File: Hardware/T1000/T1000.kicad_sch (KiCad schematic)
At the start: 8 parts, among them J7 Micro_SD_Card_Det1, U1 SAM-M8Q, U6 MS5607-02BA

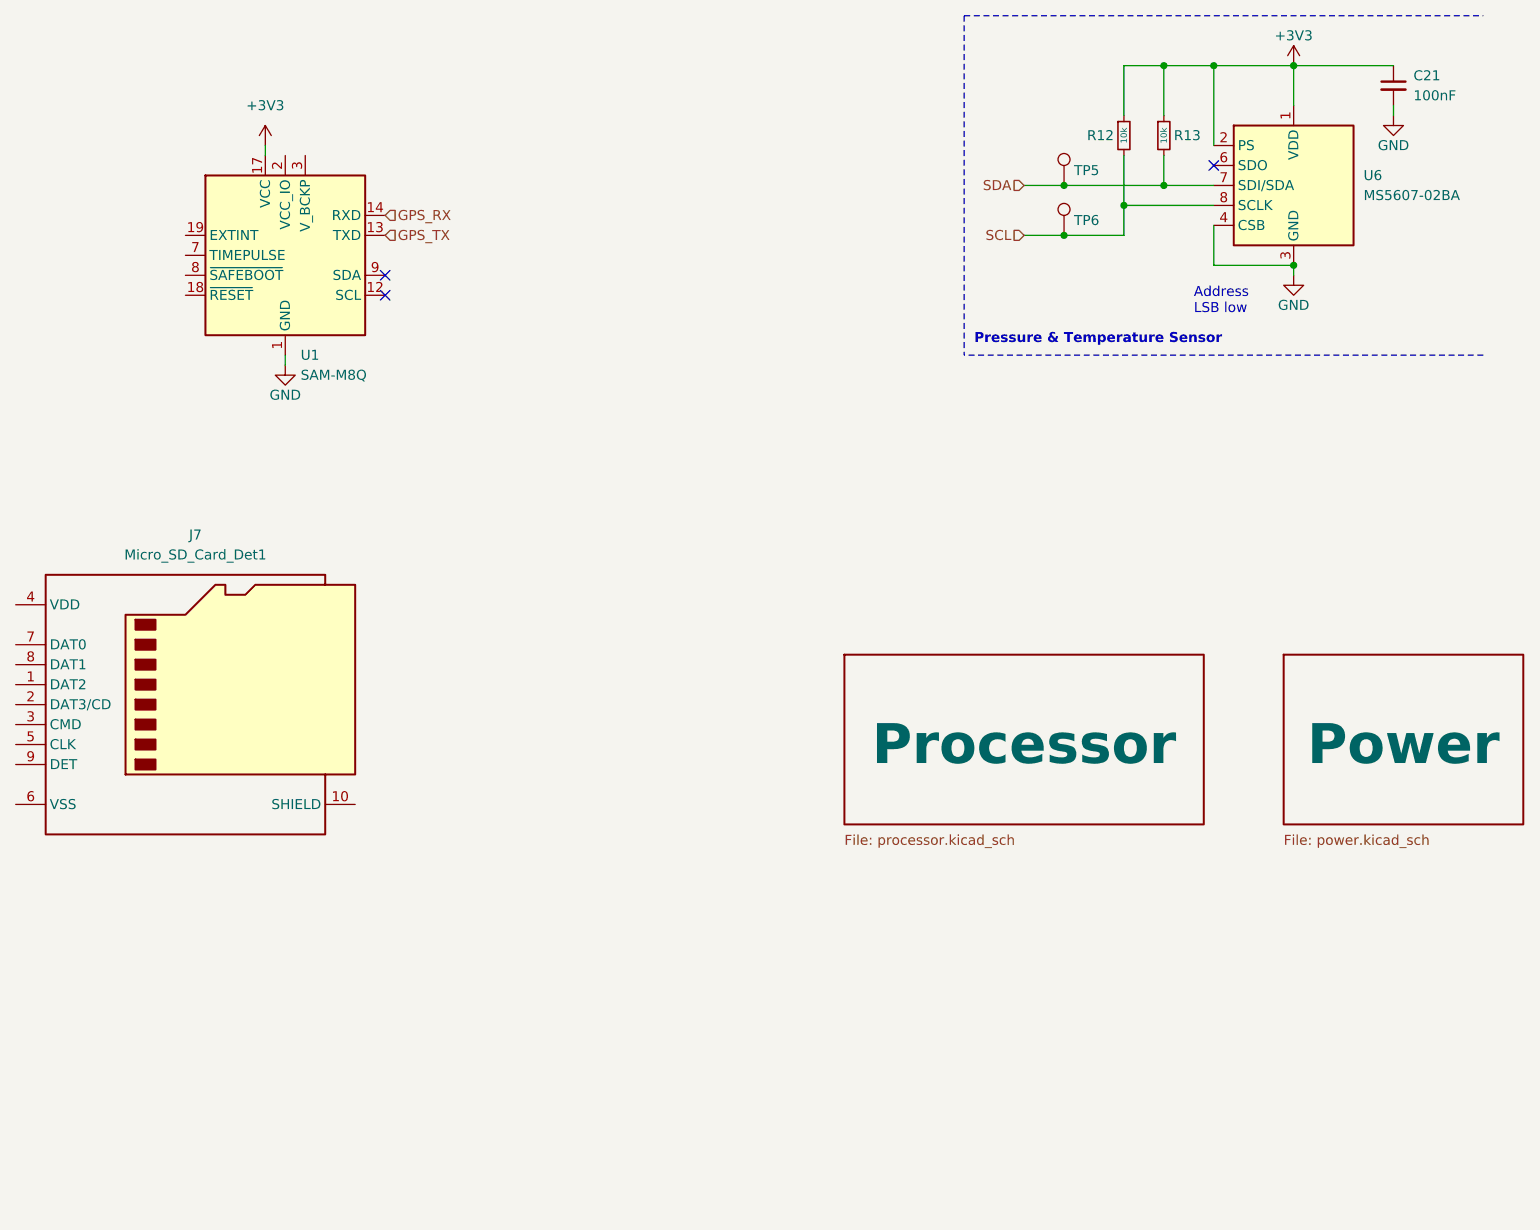
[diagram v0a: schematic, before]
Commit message: added SD card
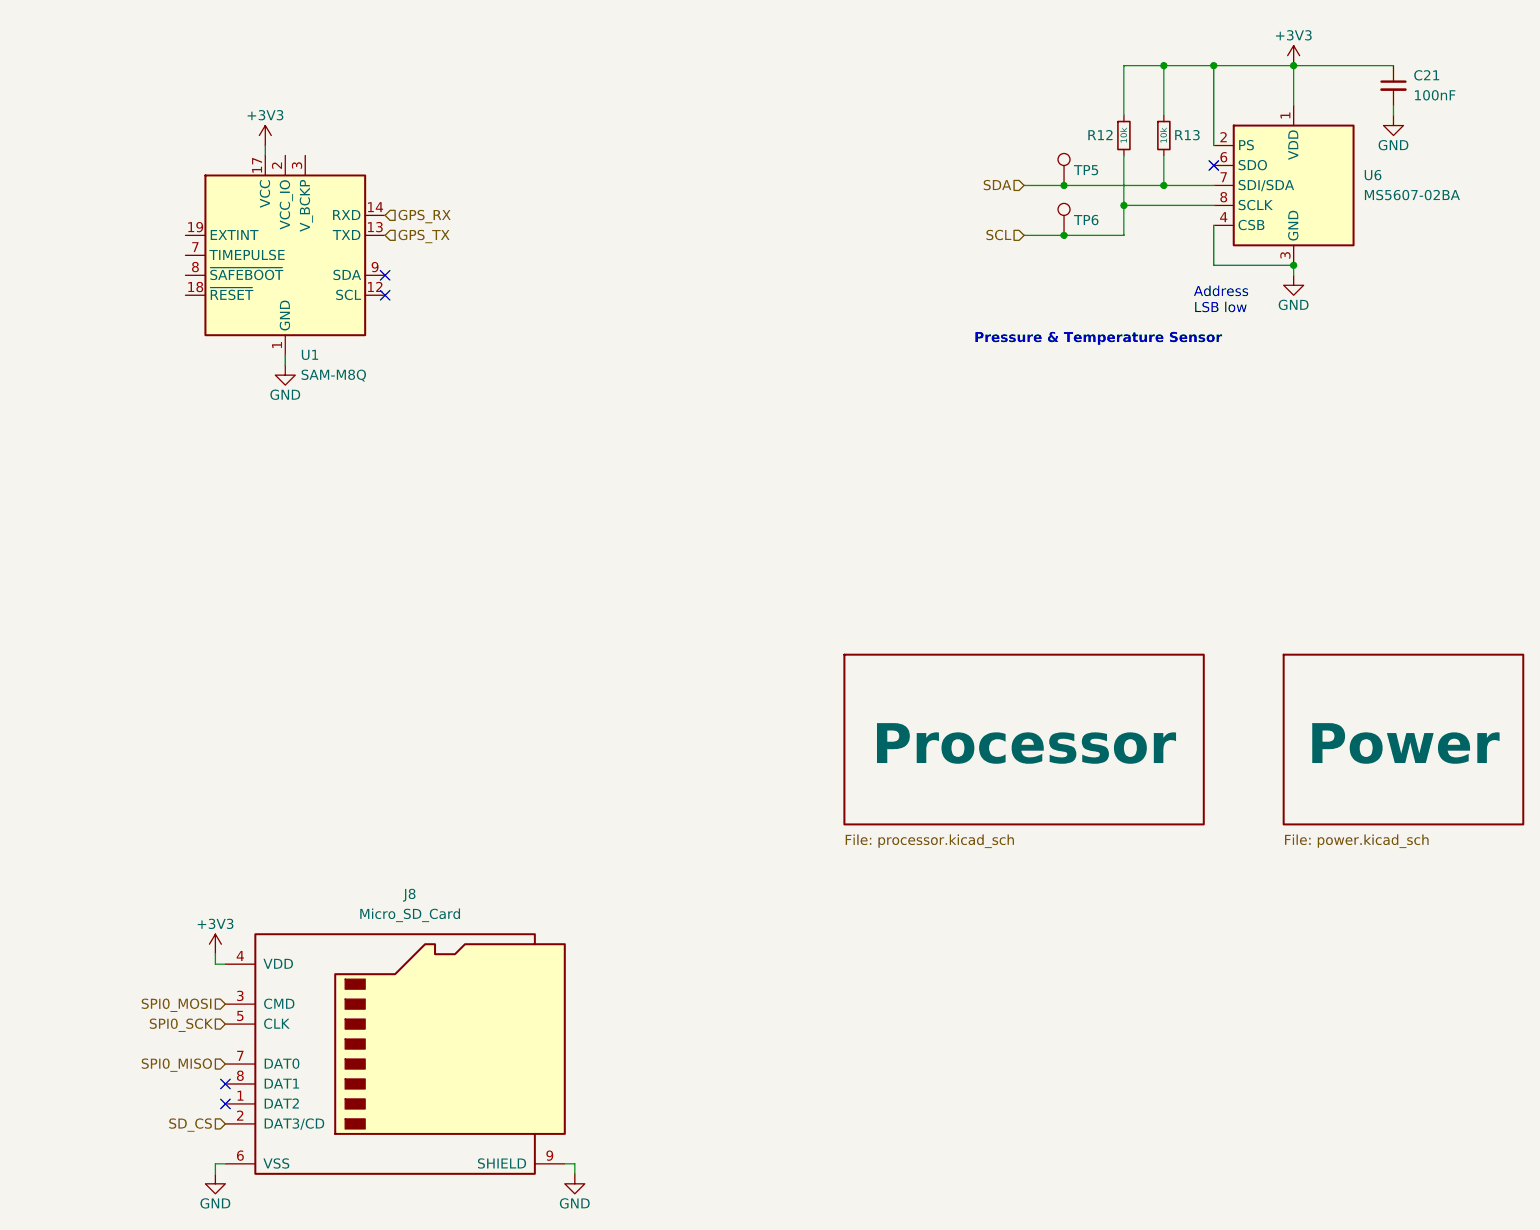
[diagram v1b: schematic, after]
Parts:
- removed J7: Micro_SD_Card_Det1, symbol Connector:Micro_SD_Card_Det1
- added J8: Micro_SD_Card, symbol Connector:Micro_SD_Card
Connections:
- net +3V3: now also J8.4 (VDD)
- net GND: now also J8.6 (VSS), J8.9 (SHIELD)
- new net SD_CS: J8.2 (DAT3/CD)
- new net SPI0_MISO: J8.7 (DAT0)
- new net SPI0_MOSI: J8.3 (CMD)
- new net SPI0_SCK: J8.5 (CLK)
- no-connect marks 3 -> 5

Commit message: schematic updates
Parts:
- removed J8: Micro_SD_Card, symbol Connector:Micro_SD_Card
- removed U1: SAM-M8Q, RF_GPS:ublox_SAM-M8Q, symbol RF_GPS:SAM-M8Q
- added AE1: Antenna, symbol Device:Antenna
- added B1, B2: KMR2, Button_Switch_SMD:SW_Push_1P1T_NO_CK_KMR2, symbol Switch:SW_Push
- added C1, C10, C12, C13, C14, C4, C7, C8, C9: 100nF, Capacitor_SMD:C_0402_1005Metric_Pad0.74x0.62mm_HandSolder, symbol Device:C_Small
- added C11: 2.2uF, Capacitor_SMD:C_0603_1608Metric_Pad1.08x0.95mm_HandSolder, symbol Device:C_Small
- added C15, C18: 10uF, Capacitor_SMD:C_0603_1608Metric_Pad1.08x0.95mm_HandSolder, symbol Device:C_Small
- added C16: 100nF, Capacitor_SMD:C_0603_1608Metric_Pad1.08x0.95mm_HandSolder, symbol Device:C_Small
- added C17: 1uF, symbol Device:C_Small
- added C19, C20, C27, C28: 10uF, symbol Device:C_Small
- added C2, C3: 22pF, Capacitor_SMD:C_0603_1608Metric_Pad1.08x0.95mm_HandSolder, symbol Device:C_Small
- added C22, C23: 220nF, symbol Device:C_Small
- added C24: 10pF, symbol Device:C_Small
- added C25: 2.2uF, symbol Device:C_Small
- added C26: 470nF, symbol Device:C_Small
- added C29: C_Small, symbol Device:C_Small
- added C5, C6: 1uF, Capacitor_SMD:C_0402_1005Metric_Pad0.74x0.62mm_HandSolder, symbol Device:C_Small
- added D1: LED, Diode_SMD:D_0603_1608Metric_Pad1.05x0.95mm_HandSolder, symbol Device:LED
- added D2: USBLC6-2SC6, Package_TO_SOT_SMD_AKL:SOT-23-6, symbol Diode_TVS_AKL:USBLC6-2SC6
- added J1: USB_C_Receptacle_USB2.0, Connector_USB:USB_C_Receptacle_GCT_USB4085, symbol Connector:USB_C_Receptacle_USB2.0
- added J2: SOICbite, Connector:SOIC_clipProgSmall, symbol Connector:Conn_01x08_Female
- added L1: 1.5uH, symbol Device:L
- added L2: L_Small, symbol Device:L_Small
- added L3: L, symbol Device:L
- added Q1: IRLML0060TRPBF, Package_TO_SOT_SMD:SOT-23-3, symbol Device:Q_NMOS_GSD
- added R1: DNP, Resistor_SMD:R_0603_1608Metric_Pad0.98x0.95mm_HandSolder, symbol Device:R_Small
- added R10: 154k, symbol Device:R_Small
- added R11, R2: 10k, Resistor_SMD:R_0603_1608Metric_Pad0.98x0.95mm_HandSolder, symbol Device:R_Small
- added R14, R15: 5.1k, Resistor_SMD:R_0603_1608Metric_Pad0.98x0.95mm_HandSolder, symbol Device:R_Small
- added R16: 510k, symbol Device:R_Small
- added R17: 16.9k, symbol Device:R_Small
- added R18: 178k, symbol Device:R_Small
- added R19: 20k, symbol Device:R_Small
- added R20: 100m, symbol Device:R_Small
- added R21, R22: 33, symbol Device:R_Small
- added R3: 1M, Resistor_SMD:R_0603_1608Metric_Pad0.98x0.95mm_HandSolder, symbol Device:R_Small
- added R4: 715k, Resistor_SMD:R_0603_1608Metric_Pad0.98x0.95mm_HandSolder, symbol Device:R_Small
- added R5, R6: 27, Resistor_SMD:R_0603_1608Metric_Pad0.98x0.95mm_HandSolder, symbol Device:R_Small
- added R7: 590, Resistor_SMD:R_0603_1608Metric_Pad0.98x0.95mm_HandSolder, symbol Device:R_Small
- added R8: 1k, Resistor_SMD:R_0603_1608Metric_Pad0.98x0.95mm_HandSolder, symbol Device:R_Small
- added R9: 1.05M, symbol Device:R_Small
- added TP1, TP3, TP4: TestPoint, TestPoint:TestPoint_Pad_D1.0mm, symbol Connector:TestPoint
- added TP2: TestPoint, TestPoint:TestPoint_Keystone_5000-5004_Miniature, symbol Connector:TestPoint
- added U2: RP2040, RP2040_minimal:RP2040-QFN-56, symbol MCU_RaspberryPi:RP2040
- added U3: W25Q128JVS, Package_SO:SOIC-8_5.23x5.23mm_P1.27mm, symbol Memory_Flash:W25Q128JVS
- added U4: LTC4419, Package_SO:MSOP-12-1EP_3x4mm_P0.65mm_EP1.65x2.85mm_ThermalVias, symbol Power_Management:LTC4419
- added U5: MAX-M10S, RF_GPS:ublox_MAX, symbol RF_GPS:MAX-M10S
- added U7: LT6703CDC-3, Package_DFN_QFN_AKL:DFN-3-1EP-2x2mm_P0.5mm_EP1x1.35mm, symbol PCM_Analog_Comparator_AKL:LT6703CDC-3
- added U8: MAX77857, MAX77857:MAX77857-35WLP, symbol Power_Management:MAX77857BEWB+
- added Y1: 445I23D12M00000, Crystal:Crystal_SMD_5032-2Pin_5.0x3.2mm, symbol Device:Crystal_Small
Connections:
- net +3V3: now also C10.1, C12.1, C13.1, C14.1, C15.1, C16.1, C24.1, C27.1, C28.1, C29.1, C6.1, C7.1, C8.1, C9.1, J2.1 (Pin_1), L2.1, L3.1, L3.2, Q1.3 (D), R11.1, R18.1, R2.1, R20.2, U2.1 (IOVDD), U2.10 (IOVDD), U2.22 (IOVDD), U2.33 (IOVDD), U2.42 (IOVDD), U2.43 (ADC_AVDD), U2.44 (VREG_IN), U2.48 (USB_VDD), U2.49 (IOVDD), U3.8 (VCC), U5.6 (V_BCKP), U5.7 (VCC_IO), U5.8 (VCC), U8.D4 (OUT), U8.E4 (OUT), U8.E5 (OUT), U8.E6 (OUT)
- net GND: now also B1.1, B2.1, C1.2, C10.2, C11.2, C12.2, C13.2, C14.2, C15.2, C16.2, C17.2, C18.2, C19.2, C2.1, C20.2, C25.2, C26.2, C27.2, C28.2, C29.2, C3.1, C4.2, C5.2, C6.2, C7.2, C8.2, C9.2, D1.1 (K), D2.2 (VN), J1.A1 (GND), J1.A12 (GND), J1.B1 (GND), J1.B12 (GND), J2.4 (Pin_4), R10.2, R14.2, R15.2, R17.1, R19.2, R4.2, TP2.1, U2.19 (TESTEN), U2.57 (GND), U3.4 (GND), U4.10 (CMP2), U4.11 (NC), U4.13 (GND), U4.3 (CMP1), U4.5 (GND), U5.1 (GND), U5.10 (GND), U5.12 (GND), U7.4 (V-), U8.C3 (PGND), U8.C4 (PGND), U8.C5 (PGND), U8.C6 (PGND), U8.C7 (PGND), U8.D2 (PGND), U8.D3 (PGND), U8.E2 (AGND)
- net GPS_RX: now also R21.1
- net GPS_TX: now also R22.1
- net SCL: now also U2.7 (GPIO5)
- net SDA: now also U2.6 (GPIO4)
- net SD_CS: now also U2.28 (GPIO17)
- net SPI0_MISO: now also U2.27 (GPIO16)
- net SPI0_MOSI: now also U2.30 (GPIO19)
- net SPI0_SCK: now also U2.29 (GPIO18)
- new net: J1.A5 (CC1), R14.1
- new net: D2.6 (L1), J1.A6 (D+), J1.B6 (D+)
- new net: D2.4 (L2), J1.A7 (D-), J1.B7 (D-)
- new net: J1.B5 (CC2), R15.1
- new net: R6.1, U2.46 (USB_DM)
- new net: AE1.1 (A), U5.11 (RF_IN)
- new net: R16.2, U7.1 (OUT), U8.B2 (EN), U8.B3 (EN)
- new net: C24.2, R18.2, R19.1, U8.E1 (FB)
- new net: C22.1, U8.A3 (BST1)
- new net: C22.2, L1.1, U8.A7 (LX1), U8.B5 (LX1), U8.B6 (LX1), U8.B7 (LX1)
- new net: C2.2, U2.20 (XIN), Y1.2
- new net: R1.2, U2.21 (XOUT)
- new net: J2.2 (Pin_2), U2.24 (SWCLK)
- new net: J2.3 (Pin_3), U2.25 (SWD)
- new net: B1.2, R2.2, U2.26 (RUN)
- new net: R5.1, U2.47 (USB_DP)
- new net: D1.2 (A), R7.2
- new net: R10.1, R9.2, U7.3 (IN+)
- new net: C25.1, C26.1, U8.A1 (SCL), U8.A2 (VIO), U8.B1 (SDA), U8.C1 (VL)
- new net: R22.2, U5.2 (TXD)
- new net: R21.2, U5.3 (RXD)
- new net: R17.2, U8.D1 (SEL)
- new net: B2.2, R8.1
- new net: R3.2, R4.1, U4.4 (ADJ)
- new net: C23.1, L1.2, U8.D5 (LX2), U8.D6 (LX2), U8.D7 (LX2), U8.E7 (LX2)
- new net: C23.2, U8.E3 (BST2)
- new net: C3.2, R1.1, Y1.1
- new net: Q1.2 (S), R7.1
- new net: L2.2, R20.1
- new net +1V1: C1.1, C4.1, C5.1, U2.23 (DVDD), U2.45 (VREG_VOUT), U2.50 (DVDD)
- new net +BATT: C11.1, C17.1, R16.1, R3.1, R9.1, U4.1 (V1), U7.2 (V+)
- new net D1: Q1.1 (G), U2.11 (GPIO8)
- new net QSPI_SCLK: U2.52 (QSPI_SCLK), U3.6 (CLK)
- new net QSPI_SD0: U2.53 (QSPI_SD0), U3.5 (DI(IO0))
- new net QSPI_SD1: U2.55 (QSPI_SD1), U3.2 (DO(IO1))
- new net QSPI_SD2: U2.54 (QSPI_SD2), U3.3 (IO2)
- new net QSPI_SD3: U2.51 (QSPI_SD3), U3.7 (IO3)
- new net QSPI_SS: R11.2, R8.2, U2.56 (QSPI_SS), U3.1 (~{CS})
- new net SRC: C18.1, C19.1, C20.1, U4.9 (OUT), U8.A4 (IN), U8.A5 (IN), U8.A6 (IN), U8.B4 (IN)
- new net USB_D+: D2.1 (L1), R5.2, TP3.1
- new net USB_D-: D2.3 (L2), R6.2, TP4.1
- new net VBUS: D2.5 (VP), J1.A4 (VBUS), J1.A9 (VBUS), J1.B4 (VBUS), J1.B9 (VBUS), TP1.1, U4.12 (V2)
- no-connect marks 5 -> 44
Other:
- removed sheet Power
- removed sheet Processor
- note added: "DNF"
- note added: "GPS"
- note added: "Low Voltage Cutoff"
- note added: "Make sure C10 is close to pin 44 of RP2040"
- note added: "Make sure C8 is close to pin 45 of RP2040"
- note added: "Make sure R3 and R4 are close to RP2040"
- note added: "Power Source Switching"
- note added: "This resistor ensures that we don't overdrive the LED"
- note added: "Transient Voltage Suppression"
- note added: "USB"
- moved on the sheet: C21, R12, R13, TP5, TP6, U6

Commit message: filter tuning
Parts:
- removed L2: L_Small, symbol Device:L_Small
- added C30: 10uF, symbol Device:C_Small
- added C31: 2.2uF, Capacitor_SMD:C_0603_1608Metric_Pad1.08x0.95mm_HandSolder, symbol Device:C_Small
- added C35: 100nF, symbol Device:C_Small
- added C36: 47pF, symbol Device:C_Small
- added C37: 8.2pF, symbol Device:C_Small
- added J3: XT30, symbol Connector:Conn_01x02_Pin
- added R23: 0, symbol Device:R_Small
- added U9: XBee_SMT, RF_Module:Digi_XBee_SMT, symbol RF_ZigBee:XBee_SMT
- C29: value C_Small -> 15uF
- L3: value L -> 3.3uH
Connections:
- net +3V3: now also R20.1, R7.1, C30.1, C35.1, C36.1, C37.1, U9.2 (VCC); no longer Q1.3 (D)
- net +BATT: now also J3.1 (Pin_1); no longer C17.1, R16.1, R9.1, U7.2 (V+)
- net GND: now also Q1.2 (S), C30.2, C31.2, C35.2, C36.2, C37.2, J3.2 (Pin_2), R23.2, U9.1 (GND), U9.11 (GND), U9.13 (GND), U9.22 (GND), U9.35 (GND); no longer D1.1 (K)
- net VBUS: now also C31.1
- net at J1.S1 (SHIELD): now also R23.1
- net SRC renamed +VDC
- net +VDC: now also C17.1, R16.1, R9.1, U7.2 (V+)
- new net: D1.1 (K), Q1.3 (D)
- new net XBEE_DTR: U9.10 (DIO8/SLEEP_REQUEST)
- new net XBEE_RTS: U9.29 (DIO6/~{RTS})
- new net XBEE_RX: U9.4 (DIO14/UART_RX/~{CONFIG})
- new net XBEE_TX: U9.3 (DIO13/UART_TX)
- no-connect marks 44 -> 62
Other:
- note added: "Microcontroller"
- note added: "Output Filter"
- note added: "Power Management"
- note added: "XBee"
- moved on the sheet: AE1, B1, B2, C11, C16, C17, C18, C19, C2, C20, C21, C22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

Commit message: started layout
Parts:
- added BZ1: Buzzer, Terminator_Lib:PKMCS0909E4000-R1_MUR, symbol Device:Buzzer
- added C32, C33: 220nF, Capacitor_SMD:C_0603_1608Metric_Pad1.08x0.95mm_HandSolder, symbol Device:C_Small
- added C34: 4.7uF, Capacitor_SMD:C_0603_1608Metric_Pad1.08x0.95mm_HandSolder, symbol Device:C_Small
- added C38: 22nF, Capacitor_SMD:C_0603_1608Metric_Pad1.08x0.95mm_HandSolder, symbol Device:C_Small
- added C39, C40: 22uF, Capacitor_SMD:C_0603_1608Metric_Pad1.08x0.95mm_HandSolder, symbol Device:C_Small
- added C41: 680p, Capacitor_SMD:C_0603_1608Metric_Pad1.08x0.95mm_HandSolder, symbol Device:C_Small
- added C42: 10uF, Capacitor_SMD:C_0603_1608Metric_Pad1.08x0.95mm_HandSolder, symbol Device:C_Small
- added J4: Nichrome, Connector_PinHeader_2.54mm:PinHeader_1x02_P2.54mm_Vertical, symbol Connector:Conn_01x02_Socket
- added JP1, JP2: SolderJumper_2_Open, Jumper:SolderJumper-2_P1.3mm_Open_TrianglePad1.0x1.5mm, symbol Jumper:SolderJumper_2_Open
- added L2: 3.3uH, Terminator_Lib:L_Bourns_SRP1265A, symbol Device:L
- added R24: 75k, Resistor_SMD:R_0603_1608Metric_Pad0.98x0.95mm_HandSolder, symbol Device:R_Small
- added R25: 5m, Resistor_SMD:R_0603_1608Metric_Pad0.98x0.95mm_HandSolder, symbol Device:R_Small
- added R26, R27: 154k, Resistor_SMD:R_0603_1608Metric_Pad0.98x0.95mm_HandSolder, symbol Device:R_Small
- added R28: 56.2k, Resistor_SMD:R_0603_1608Metric_Pad0.98x0.95mm_HandSolder, symbol Device:R_Small
- added R29: 100, Resistor_SMD:R_0603_1608Metric_Pad0.98x0.95mm_HandSolder, symbol Device:R_Small
- added U1: LT3120JV-PBF, Terminator_Lib:LQFN28_Rev0_ADI-M, symbol Terminator_Lib:LT3120JV-PBF
- AE1: footprint (none) -> Terminator_Lib:ANT_1575AT_JOT-M
- C17, C19, C20, C22, C23, C24, C25, C26, C27, C28, C29, C30, C35, C36, C37: footprint (none) -> Capacitor_SMD:C_0603_1608Metric_Pad1.08x0.95mm_HandSolder
- D2: footprint Package_TO_SOT_SMD_AKL:SOT-23-6 -> PCM_Package_TO_SOT_SMD_AKL:SOT-23-6
- J2: footprint Connector:SOIC_clipProgSmall -> Terminator_Lib:SOIC_clipProgSmall
- J3: footprint (none) -> Connector_AMASS:AMASS_XT30PW-M_1x02_P2.50mm_Horizontal
- L1: footprint (none) -> Inductor_SMD:L_Vishay_IHLP-2020
- L3: footprint (none) -> Terminator_Lib:L_Bourns_SRP1265A
- R10, R16, R17, R18, R19, R20, R21, R22, R9: footprint (none) -> Resistor_SMD:R_0603_1608Metric_Pad0.98x0.95mm_HandSolder
- R23: value 0 -> 81.1k; footprint (none) -> Resistor_SMD:R_0603_1608Metric_Pad0.98x0.95mm_HandSolder
- U2: footprint RP2040_minimal:RP2040-QFN-56 -> Terminator_Lib:RP2040-QFN-56
- U7: footprint Package_DFN_QFN_AKL:DFN-3-1EP-2x2mm_P0.5mm_EP1x1.35mm -> PCM_Package_DFN_QFN_AKL:DFN-3-1EP-2x2mm_P0.5mm_EP1x1.35mm
- U8: footprint MAX77857:MAX77857-35WLP -> Terminator_Lib:MAX77857-35WLP
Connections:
- net +3V3: now also JP2.1 (A); no longer C24.1, C27.1, C28.1, L3.1, R18.1, R20.1, U8.D4 (OUT), U8.E4 (OUT), U8.E5 (OUT), U8.E6 (OUT)
- net +BATT: now also JP1.1 (A), R25.1, U1.5 (ISP)
- net GND: now also J1.S1 (SHIELD), BZ1.2 (+), C34.2, C39.2, C40.2, C41.2, C42.2, J4.2 (Pin_2), R24.2, R27.2, U1.11 (GND), U1.18 (GND), U1.22 (GND), U1.29 (PGND), U1.3 (GND)
- net at R23.1: now also U1.8 (PROG); no longer J1.S1 (SHIELD)
- net LVC: now reaches R16.2, U7.1 (OUT), U8.B2 (EN), U8.B3 (EN)
- net LVC: now also U1.16 (EN/UVLO)
- net at U2.13 (GPIO10): now also R29.1
- new net: BZ1.1 (-), R29.2
- new net: JP1.2 (B), JP2.2 (B), U1.17 (VIN)
- new net: C38.1, U1.1 (BST3)
- new net: R28.1, U1.10 (VC)
- new net: C34.1, U1.12 (MPCC), U1.13 (VCC)
- new net: R24.1, U1.14 (RT)
- new net: C42.1, R25.2, U1.15 (SYNC/MODE), U1.19 (PVIN), U1.20 (PVIN), U1.21 (PVIN), U1.6 (ISN)
- new net: C38.2, C39.1, C40.1, J4.1 (Pin_1), R26.1, U1.2 (PVOUT), U1.4 (PVOUT)
- new net: C32.1, U1.23 (BST1)
- new net: C32.2, L2.1, U1.24 (SW1), U1.25 (SW1)
- new net: C33.2, L2.2, U1.26 (SW2), U1.27 (SW2)
- new net: C33.1, U1.28 (BST2)
- new net: R26.2, R27.1, U1.9 (FB)
- new net: C24.1, C27.1, C28.1, L3.1, R18.1, R20.1, U8.D4 (OUT), U8.E4 (OUT), U8.E5 (OUT), U8.E6 (OUT)
- new net: C41.1, R28.2
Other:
- note added: "Battery Connector"
- note added: "Cutdown Circuit"
- note added: "Power Path Switching"
- note removed: "Power Source Switching"
- moved on the sheet: AE1, C11, C17, C18, C19, C20, C21, C22, C23, C24, C25, C26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

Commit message: more layout
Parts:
- C29: footprint Capacitor_SMD:C_0603_1608Metric_Pad1.08x0.95mm_HandSolder -> Capacitor_SMD:C_0805_2012Metric_Pad1.18x1.45mm_HandSolder
- L3: footprint Terminator_Lib:L_Bourns_SRP1265A -> Inductor_SMD:L_1008_2520Metric_Pad1.43x2.20mm_HandSolder
- R20: footprint Resistor_SMD:R_0603_1608Metric_Pad0.98x0.95mm_HandSolder -> Resistor_SMD:R_0805_2012Metric_Pad1.20x1.40mm_HandSolder
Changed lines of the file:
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@@
       (effects (font (size 1.27 1.27)))
     )
-    (property "Footprint" "Terminator_Lib:L_Bourns_SRP1265A" (at 270.51 185.42 0)
+    (property "Footprint" "Inductor_SMD:L_1008_2520Metric_Pad1.43x2.20mm_HandSolder" (at 270.51 185.42 0)
       (effects (font (size 1.27 1.27)) hide)
     )
@@
       (effects (font (size 1.27 1.27)) (justify left))
     )
-    (property "Footprint" "Capacitor_SMD:C_0603_1608Metric_Pad1.08x0.95mm_HandSolder" (at 276.86 189.23 0)
+    (property "Footprint" "Capacitor_SMD:C_0805_2012Metric_Pad1.18x1.45mm_HandSolder" (at 276.86 189.23 0)
       (effects (font (size 1.27 1.27)) hide)
     )
@@
       (effects (font (size 0.7 0.7)))
     )
-    (property "Footprint" "Resistor_SMD:R_0603_1608Metric_Pad0.98x0.95mm_HandSolder" (at 270.51 181.61 0)
-      (effects (font (size 1.27 1.27)) hide)
-    )
+    (property "Footprint" "Resistor_SMD:R_0805_2012Metric_Pad1.20x1.40mm_HandSolder" (at 270.51 181.61 0)
+      (effects (font (size 1.27 1.27)) hide)
+    )
